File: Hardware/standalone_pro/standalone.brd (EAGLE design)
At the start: 110.2 x 100 mm, 111 parts, among them IC1 STM32F050C6T6A, IC2 AP1212, IC3 IR2104S, IC4 AP1212, Q1 32.768khz, U10 ZXCT1107SA-7, U11 NMOS_2N7002, U12 NMOS_2N7002, U2 FDS6690a, U3 FDS6690a, U4 LM2576S, U5 NMOS_2N7002, U6 NMOS_2N7002, U7 INA213AIDCKT, U8 NMOS_2N7002, X1 KUSBVX, X2 KUSBVX, X3 KUSBVX, X4 KUSBVX

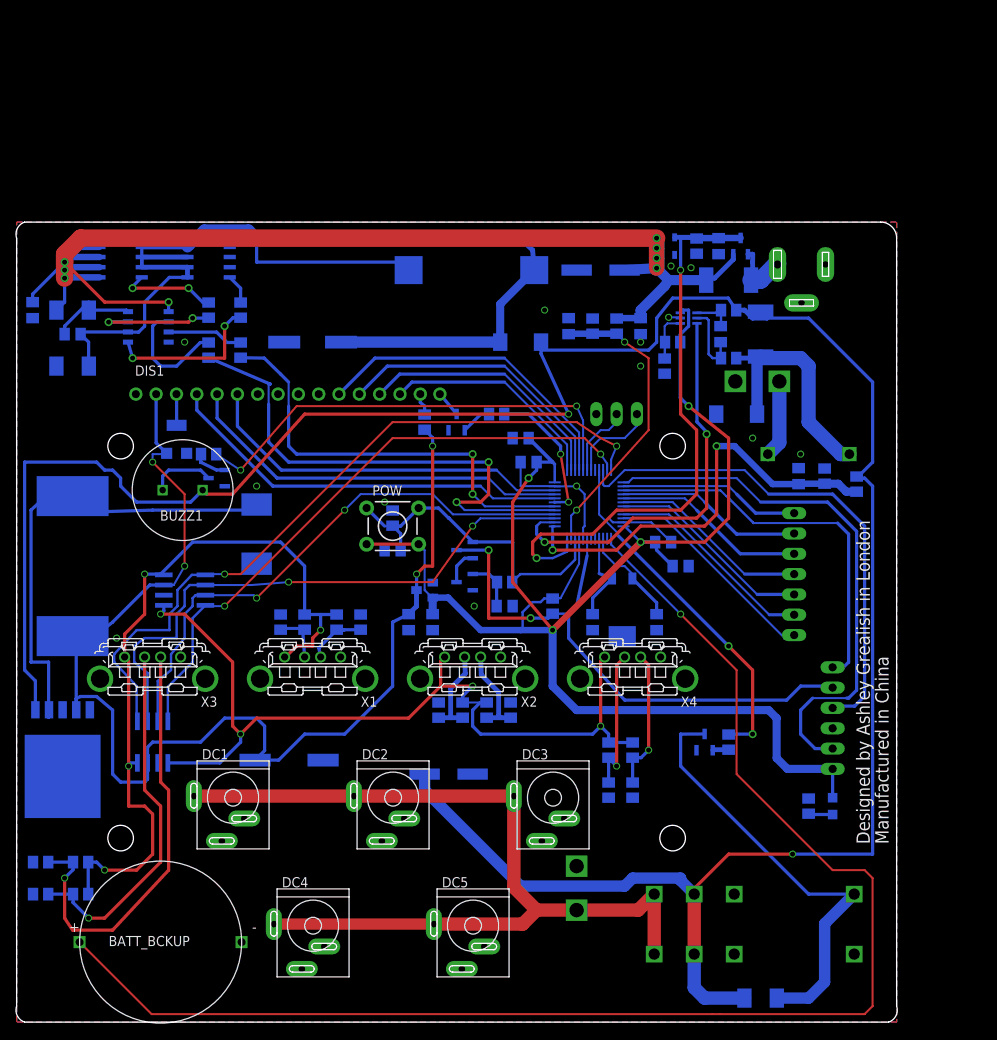
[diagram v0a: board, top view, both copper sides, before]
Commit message: Changed RTC XTAL Hardware
Both Home and Pro boards have working XTAL. OC_FARNELL attributes give
correct part numbers.
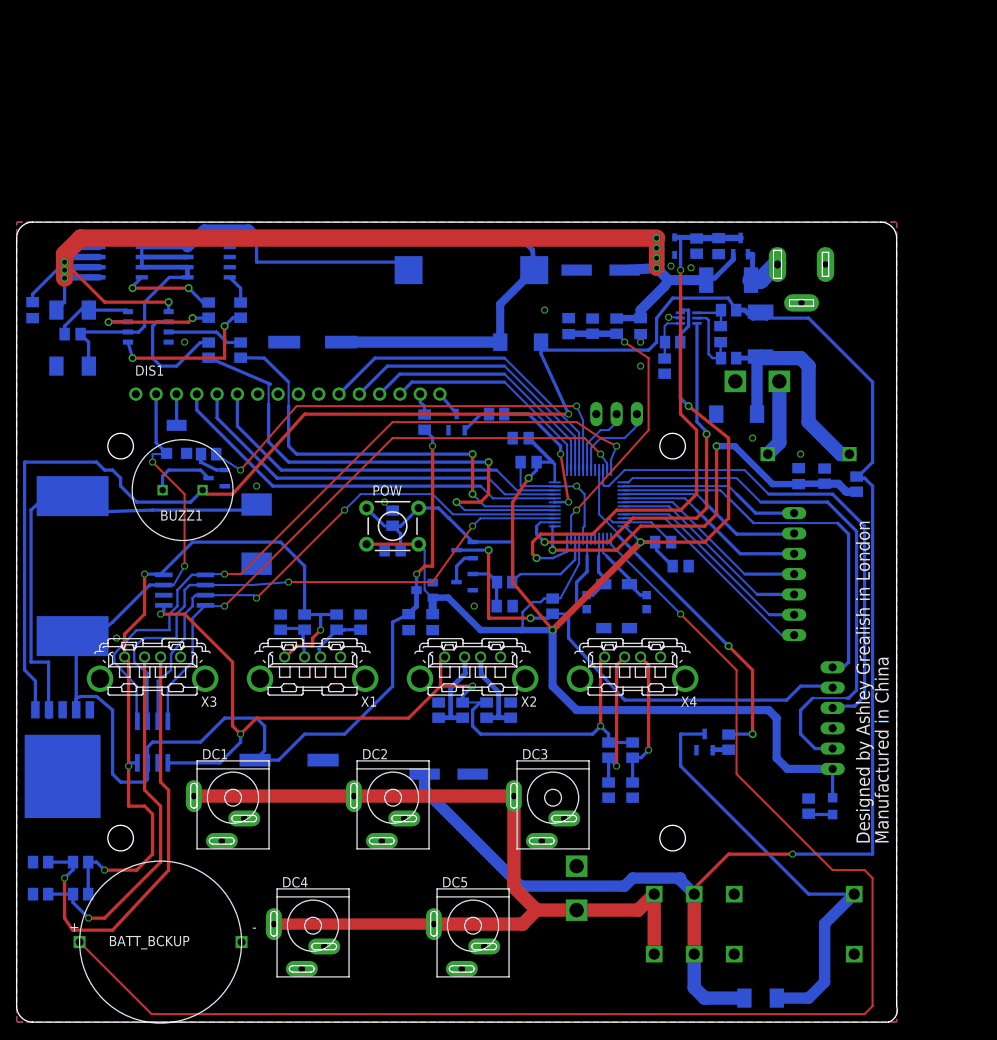
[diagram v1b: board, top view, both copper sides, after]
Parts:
- removed C1, C9: 12.5pF, resistor:C0805K
- removed Q1: 32.768khz, equinox:CRYSTAL_CMJ206T
- added C23, C24: 6.8pF, resistor:C0603K
- added Q2: 32.768kHz, crystal:MC-306
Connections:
- removed net N$18: C9.2, IC1.4, Q1.P$3
- new net N$49: C24.2, IC1.4, Q2.4
- net GND: now also C23.1, C24.1; no longer C1.1, C9.1, Q1.CASE
- net N$1: now also C23.2, Q2.1; no longer C1.2, Q1.P$2
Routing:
- net N$18: track 11.5 -> 0.00 mm
- net N$49: track 0.00 -> 8.68 mm
- net N$1: track 12.8 -> 9.75 mm
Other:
- board size 110.2 x 100 mm -> 110.1 x 100 mm

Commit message: Pro Unit Hardware design completed
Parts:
- removed C23, C24: 6.8pF, resistor:C0603K
- removed U11, U12, U8: NMOS_2N7002, equinox:SOT103P240X110-3N
- added C1, C9: 1uF, resistor:C0805K
- added R14: 1.33k, rcl:M0805
- added T1: (no value), transistor:SOT23-BEC
- added U1: ZXCT1107SA-7, equinox:SOT91P240X110-3N
- added U9: LM2576S, equinox:TO263-5
- C11, C16, C18, C2: value 1uF -> 100nF
- C12: value 1uF -> 220uF; device resistor:C0805K -> resistor:PANASONIC_F
- C13, C3: value 100nF -> 10uF
- C14, C5: value 100nF -> 1uF
- C17: value 1uF -> 10uF
- C19: value 1uF -> 100uF; device resistor:C0805K -> resistor:PANASONIC_E
- C20: value 10uF -> 1uF
- C21, C4: value 100uF -> 1uF; device resistor:PANASONIC_E -> resistor:C0805K
- C6: value 220uF -> 6.8pF; device resistor:PANASONIC_F -> resistor:C0603K
- C7: value 10uF -> 6.8pF; device resistor:C0805K -> resistor:C0603K
- C8: value 10uF -> 100uF; device resistor:C0805K -> resistor:PANASONIC_E
- CONTR: device resistor:RTRIM3304W -> equinox:R_TRIMM_RC33X
- D1: value SSB43L -> BZX384-C3V6; device equinox:DO214AA -> equinox:SOD323
- D3: value SSB43L -> US1D; device equinox:DO214AA -> diode:DO-214AC
- D4: value US1D -> SSB43L; device diode:DO-214AC -> equinox:DO214AA
- D5: value BZX384-C3V6 -> SSB43L; device equinox:SOD323 -> equinox:DO214AA
- IC1: value STM32F050C6T6A -> IR2104S; device equinox:LQFP48 -> equinox:IR2104S
- IC2: value AP1212 -> STM32F050C6T6A; device equinox:SO8 -> equinox:LQFP48
- IC3: value IR2104S -> AP1212; device equinox:IR2104S -> equinox:SO8
- L_MPPT: device equinox:INDUC_BOURNS_SDR1806 -> equinox:INDUC_MURATA_1433428C
- R1: value 75k -> 1k65; device resistor:M0805 -> rcl:M0805
- R10: value 5 -> 1k; device rcl:M0805 -> resistor:M0805
- R11: value 75k -> 200; device resistor:M0805 -> rcl:M0805
- R12: value 49.9k -> 100
- R13, R16: value 75k -> 10K; device resistor:M0805 -> rcl:M0805
- R15: value 49.9k -> 10K; device resistor:M0805 -> rcl:M0805
- R17: value 49.9k -> 10; device resistor:M0805 -> rcl:M0805
- R18: value 75k -> 10; device resistor:M0805 -> rcl:M0805
- R19: value 49.9k -> 0R
- R2: value 200 -> 1k; device rcl:M0805 -> resistor:M0805
- R20: device rcl:M0805 -> resistor:M0805
- R22: value 0R -> 1k; device resistor:M0805 -> rcl:M0805
- R23, R29: value 1k -> 75k
- R24: value 1k -> 49.9k
- R25: value 10K -> 75k; device rcl:M0805 -> resistor:M0805
- R26: value 10K -> 49.9k; device rcl:M0805 -> resistor:M0805
- R27: value 10 -> 75k; device rcl:M0805 -> resistor:M0805
- R28: value 10 -> 49.9k; device rcl:M0805 -> resistor:M0805
- R3: value 10K -> 10M; device rcl:M0805 -> resistor:M0805
- R30: value 1k65 -> 49.9k; device rcl:M0805 -> resistor:M0805
- R31: value 10M -> 75k
- R4: value 1.33k -> 10K
- R5: value 10K -> 1.33k
- R6: value 1.33k -> 200
- R8: value 200 -> 5
- U10: value ZXCT1107SA-7 -> NMOS_2N7002; device equinox:SOT91P240X110-3N -> equinox:SOT103P240X110-3N
- U2, U3: value FDS6690a -> NMOS_2N7002; device equinox:SOIC127P600X175-8N -> equinox:SOT103P240X110-3N
- U4: value LM2576S -> FDS6690a; device equinox:TO263-5 -> equinox:SOIC127P600X175-8N
- U5: value NMOS_2N7002 -> FDS6690a; device equinox:SOT103P240X110-3N -> equinox:SOIC127P600X175-8N
- moved R1 111.8 mm to (75.0, 77.0), turned to 90 degrees
- moved U5 86.3 mm to (14.0, 75.0), turned to 0 degrees
- moved R6 74.7 mm to (18.0, 64.0), turned to 90 degrees
- moved C19 74.1 mm to (44.0, 11.0), turned to 0 degrees
- moved R34 71.6 mm to (64.0, 9.00), turned to 90 degrees
- moved C10 71.0 mm to (-3.00, 66.0), turned to 180 degrees
- moved R33 67.5 mm to (64.0, 14.0), turned to 90 degrees
- moved R13 67.2 mm to (95.0, 47.2)
- moved R36 65.7 mm to (0.00, -6.00), turned to 270 degrees
- moved R35 64.2 mm to (3.00, -6.00)
- moved R27 62.6 mm to (30.0, 30.0), turned to 90 degrees
- moved R30 62.5 mm to (51.8, 19.0), turned to 270 degrees
- moved U4 62.2 mm to (3.00, 75.0), turned to 0 degrees
- moved U10 62.2 mm to (76.0, 15.0), turned to 90 degrees
- moved R17 61.8 mm to (79.0, 69.0), turned to 180 degrees
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- renumbered Q2 to Q1
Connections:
- net +3V3: now also C16.2, C21.2, IC2.24, IC2.48, IC2.9, R15.2; no longer C12.2, C13.2, IC1.24, IC1.48, IC1.9, R25.2
- net +5V: now also C20.2, CONTR.CW, IC3.7, R19.2, U9.4; no longer C17.2, CONTR.3, IC2.7, R22.2, U4.4
- net 12V_OUT_EN: now also IC2.33, R22.1; no longer IC1.33, R20.1
- net BATT_I: now also IC2.14; no longer IC1.14
- net BATT_V: now also C13.2, IC2.13, R13.1, R14.2; no longer C8.2, IC1.13, R5.1, R6.2
- net CC_EN: now also IC2.18, R6.1; no longer IC1.18, R8.1
- net CC_PWM: now also IC2.17; no longer IC1.17
- net GND: now also C1.1, C12.-, C19.-, C2.1, C20.1, C21.1, C4.1, C5.2, C6.1, C8.-, C9.1, CONTR.CCW, D3.A, IC1.4, IC2.23, IC2.44, IC2.47, IC2.8, IC3.6, R1.1, R14.1, R16.1, R2.2, R24.1, R28.1, R5.1, T1.E, U10.2, U5.1, U5.3, U9.3, U9.5, U9.6; no longer C10.2, C11.1, C12.1, C17.1, C19.1, C21.-, C23.1, C24.1, C4.-, C6.-, C8.1, CONTR.1, D4.A, IC1.23, IC1.44, IC1.47, IC1.8, IC2.6, IC3.4, R12.1, R15.1, R17.1, R19.1, R24.2, R4.1, R6.1, U11.2, U3.1, U3.3, U4.3, U4.5, U4.6, U8.2
- net LCD_BK_EN: now also IC2.19, R20.1; no longer IC1.19, R23.1
- net LCD_D4: now also IC2.28; no longer IC1.28
- net LCD_D5: now also IC2.27; no longer IC1.27
- net LCD_D6: now also IC2.26; no longer IC1.26
- net LCD_D7: now also IC2.25; no longer IC1.25
- net LCD_E: now also IC2.22; no longer IC1.22
- net LCD_RS: now also IC2.20; no longer IC1.20
- net LCD_RW: now also IC2.21; no longer IC1.21
- net N$1: now also C6.2, IC2.3; no longer C23.2, IC1.3
- net N$10: now also C10.1, IC1.8; no longer C2.1, IC3.8
- net N$11: now also R9.1, U5.4; no longer R10.1, U3.4
- net N$12: now also C12.+, D4.A, R11.1; no longer C6.+, D3.A, R2.1
- net N$13: now also IC1.5, R9.2; no longer IC3.5, R10.2
- net N$14: now also R8.1, U4.4; no longer R9.1, U2.4
- net N$15: now also C11.2, R11.2; no longer C5.2, R2.2
- net N$16: now also C5.1, C8.+, C9.2, IC1.1, R4.2, U1.2, U4.5, U4.6, U4.7, U4.8; no longer C10.1, C11.2, C4.+, IC3.1, R3.2, U10.2, U2.5, U2.6, U2.7, U2.8
- net N$17: now also R35.1, R36.2; no longer R33.1, R34.2
- net N$19: now also R19.1; no longer R22.1
- net N$2: now also CONTR.WIPE; no longer CONTR.2
- net N$20: now also R25.1, R26.2; no longer R16.1, R17.2
- net N$21: now also U9.2; no longer U4.2
- net N$22: now also IC2.29, R10.1; no longer IC1.29, R29.1
- net N$23: now also IC2.46; no longer IC1.46
- net N$24: now also IC2.45; no longer IC1.45
- net N$26: now also IC2.43; no longer IC1.43
- net N$27: now also IC2.42; no longer IC1.42
- net N$28: now also IC2.41; no longer IC1.41
- net N$29: now also IC2.40; no longer IC1.40
- net N$3: now also IC1.3, R6.2; no longer IC3.3, R8.2
- net N$30: now also IC2.38; no longer IC1.38
- net N$31: now also T1.C; no longer U6.3
- net N$32: now also R20.2, T1.B; no longer R23.2, U6.1
- net N$33: now also R23.1, R24.2; no longer R11.1, R12.2
- net N$34: now also R27.1, R28.2; no longer R13.1, R15.2
- net N$35: now also R22.2, U10.1; no longer R20.2, U5.1
- net N$36: now also R29.1, R30.2; no longer R18.1, R19.2
- net N$38: now also U1.3; no longer U10.3
- net N$39: now also R15.1, R16.2; no longer R25.1, R26.2
- net N$4: now also D5.C, R18.2; no longer D1.C, R28.2
- net N$40: now also C17.2, R17.1; no longer C20.2, R27.1
- net N$41: now also C17.1, R18.1; no longer C20.1, R28.1
- net N$42: now also R12.2, U6.3; no longer U8.3
- net N$43: now also R10.2, U6.1; no longer R29.2, U8.1
- net N$44: now also C4.2, R3.2, U3.1; no longer C16.2, R31.2, U11.1
- net N$45: now also U2.2, U3.3; no longer U11.3, U12.2
- net N$47: now also R33.1, R34.2; no longer R35.1, R36.2
- net N$49: now also C7.2, IC2.4; no longer C24.2, IC1.4
- net N$5: now also R31.1; no longer R1.1
- net N$50: now also U10.3; no longer U5.3
- net N$6: now also C10.2, C11.1, D3.C, IC1.6, U4.1, U4.2, U4.3, U5.5, U5.6, U5.7, U5.8; no longer C2.2, C5.1, D4.C, IC3.6, U2.1, U2.2, U2.3, U3.5, U3.6, U3.7, U3.8
- net N$7: now also IC1.7, R8.2; no longer IC3.7, R9.2
- net N$8: now also IC1.2; no longer IC3.2
- net NRST: now also IC2.7, U2.3; no longer IC1.7, U12.3
- net SOL_I: now also C1.2, D1.C, IC2.12, R1.2, U1.1; no longer C19.2, D5.C, IC1.12, R30.2, U10.1
- net SOL_V: now also C3.2, IC2.11, R4.1, R5.2; no longer C7.2, IC1.11, R3.1, R4.2
- net SWCLK: now also IC2.37; no longer IC1.37
- net SWDIO: now also IC2.34; no longer IC1.34
- net SWO: now also IC2.39; no longer IC1.39
- net USART1_RX: now also IC2.31; no longer IC1.31
- net USART1_TX: now also IC2.30; no longer IC1.30
- net USB_EN1: now also IC2.36, IC3.1; no longer IC1.36, IC2.1
- net USB_EN2: now also IC2.35, IC3.4; no longer IC1.35, IC2.4
- net USB_FLG1: now also IC2.15, IC3.2; no longer IC1.15, IC2.2
- net USB_FLG2: now also IC2.16, IC3.3; no longer IC1.16, IC2.3
- net USB_OUT1: now also IC3.8, R23.2, R27.2, R31.2, R35.2; no longer IC2.8, R1.2, R11.2, R13.2, R33.2
- net USB_OUT2: now also IC3.5, R25.2, R29.2, R33.2; no longer IC2.5, R16.2, R18.2, R35.2
- net V_BACKUP: now also IC2.1; no longer IC1.1
- net V_LOAD: now also C19.+, D4.C, R12.1, R13.2, R17.2, U9.1; no longer C21.+, D3.C, R27.2, R5.2, U4.1
- net WKUP: now also C2.2, IC2.10, R2.1, R3.1, U2.1; no longer C3.2, IC1.10, R24.1, R31.1, U12.1
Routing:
- net V_BACKUP: track 177.6 -> 85.2 mm
- net V_LOAD: track 316.7 -> 391.9 mm, vias 2 -> 4
- net N$6: track 77.1 -> 67.4 mm
- net SOL_V: track 37.4 -> 45.6 mm
- net N$17: track 54.6 -> 46.6 mm
- net N$5: track 45.3 -> 39.3 mm
- net N$21: track 59.6 -> 65.0 mm
- net USB_OUT1: track 95.4 -> 92.1 mm
- net N$42: track 8.22 -> 10.7 mm
- net +3V3: track 208.9 -> 209.9 mm
- net USB_FLG1: track 72.8 -> 71.8 mm
- net USB_EN1: track 90.7 -> 89.8 mm
- net N$12: track 62.3 -> 61.5 mm
- net N$50: track 54.5 -> 53.6 mm, vias 0 -> 1
- net +5V: track 153.9 -> 154.7 mm
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
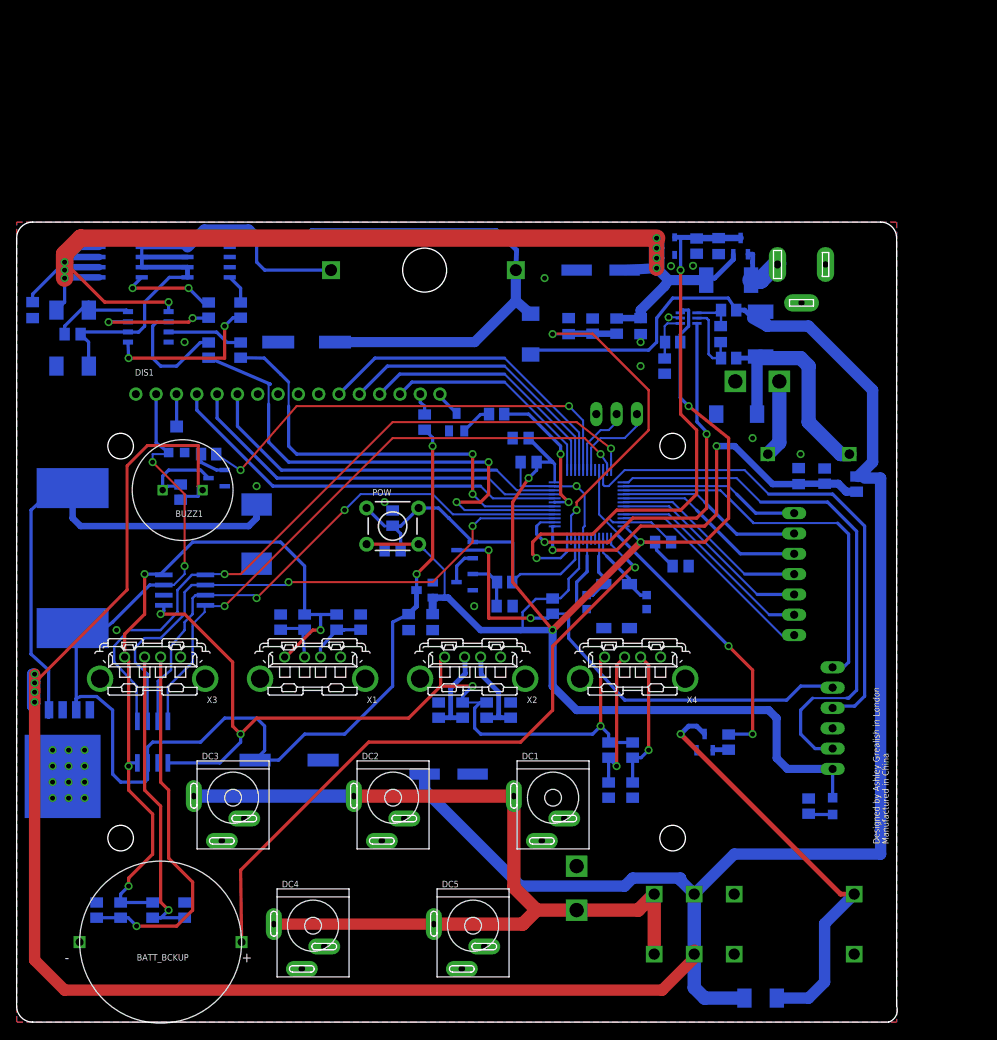
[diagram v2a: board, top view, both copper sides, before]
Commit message: Small Changes to Pro Board and Gerbers Made
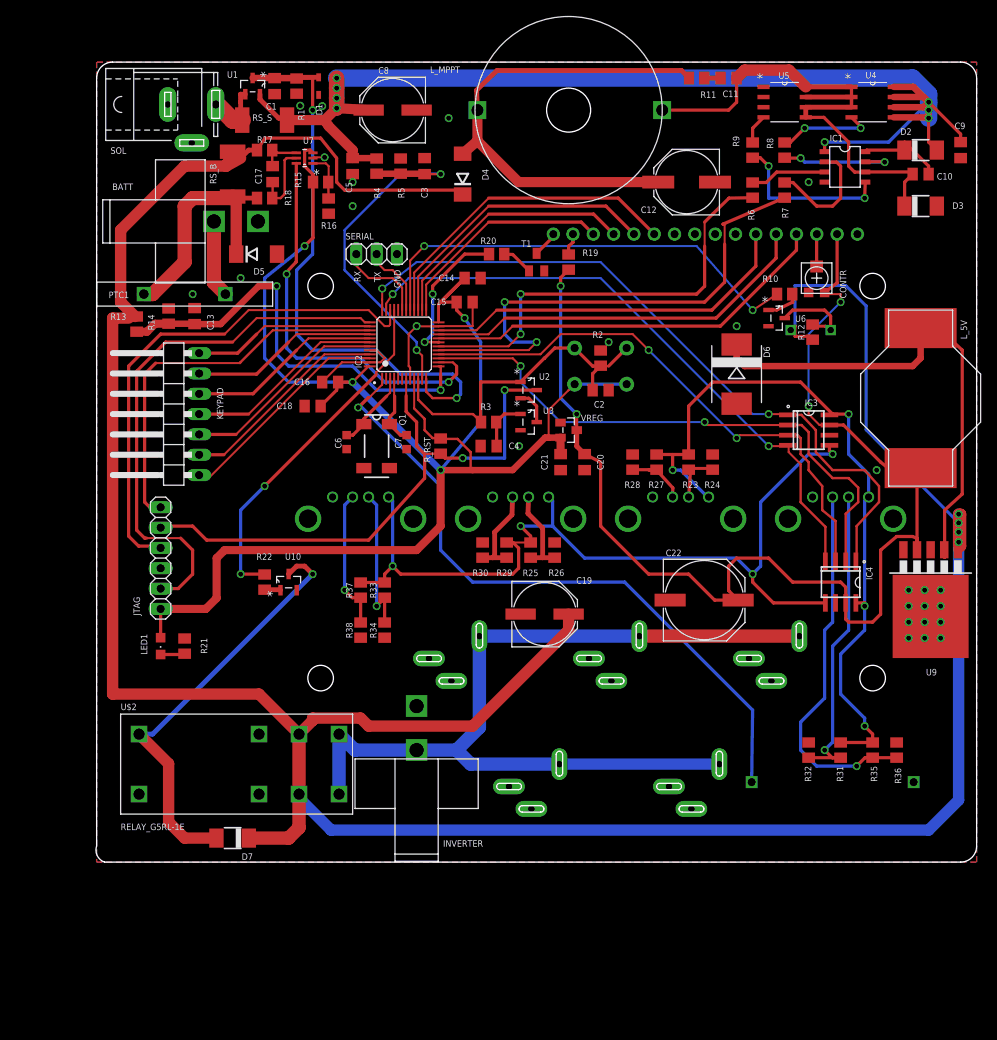
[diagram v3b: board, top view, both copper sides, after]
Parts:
- removed U$3: CON_MOLEX_39_29_1028, equinox:MOLEX_39_29_1028
- added INVERTER: CON_MOLEX_39_29_1028, equinox:MOLEX_39_29_1028
- moved C9 117.7 mm to (108.0, 89.0), flipped to the top
- moved U9 110.3 mm to (104.2, 33.2), flipped to the top
- moved DIS1 108.1 mm to (103.1, 76.0), flipped to the bottom
- moved C10 107.9 mm to (103.0, 86.0), flipped to the top
- moved D2 107.9 mm to (103.0, 89.0), flipped to the top
- moved D3 107.9 mm to (103.0, 82.0), flipped to the top
- moved L_5V 107.9 mm to (103.0, 58.0), flipped to the top
- moved R36 102.0 mm to (100.0, 14.0), flipped to the top
- moved R35 96.1 mm to (97.0, 14.0), flipped to the top
- moved U4 96.1 mm to (97.0, 95.0), flipped to the top
- moved R13 92.2 mm to (5.00, 67.2), flipped to the top
- moved IC4 88.3 mm to (93.0, 35.0), flipped to the top
- moved R31 88.3 mm to (93.0, 14.0), flipped to the top
- moved X3 88.3 mm to (93.0, 45.6), flipped to the bottom
- moved BATT_BCKUP 86.3 mm to (92.0, 10.0), flipped to the bottom
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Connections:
- net 12V_OUT: now also INVERTER.P$1; no longer U$3.P$1
- net GND: now also INVERTER.P$2; no longer U$3.P$2
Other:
- outline, holes or cut-outs redrawn

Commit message: Pro hardware ready for first prototype
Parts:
- removed PTC1: 7A, equinox:PTC_MF_R700
- moved R13 1.41 mm to (6.00, 68.2)
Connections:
- removed net N$46: BATT.P$1, PTC1.P$2
- net N$4: now also BATT.P$1; no longer PTC1.P$1
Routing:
- net +3V3: track 209.9 -> 238.3 mm
- net USB_OUT1: track 92.1 -> 120.3 mm
- net USB_OUT2: track 109.3 -> 134.5 mm
- net N$4: track 30.9 -> 14.2 mm
- net +5V: track 154.7 -> 168.2 mm
- net N$16: track 160.5 -> 172.0 mm
- net N$46: track 9.69 -> 0.00 mm
- net USB_EN2: track 77.6 -> 87.2 mm
- net N$22: track 57.0 -> 66.6 mm
- net USB_EN1: track 89.8 -> 99.4 mm
- net USB_FLG1: track 71.8 -> 81.4 mm
- net GND: track 30.9 -> 40.5 mm
- net USB_FLG2: track 69.2 -> 78.8 mm
- net SOL_V: track 45.6 -> 55.1 mm
- net CC_EN: track 54.5 -> 63.8 mm
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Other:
- board text added: "v1 - Test Board"
